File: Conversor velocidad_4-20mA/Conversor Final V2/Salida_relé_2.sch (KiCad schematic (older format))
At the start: 22 parts, among them Q2 BC848, U5 TL082

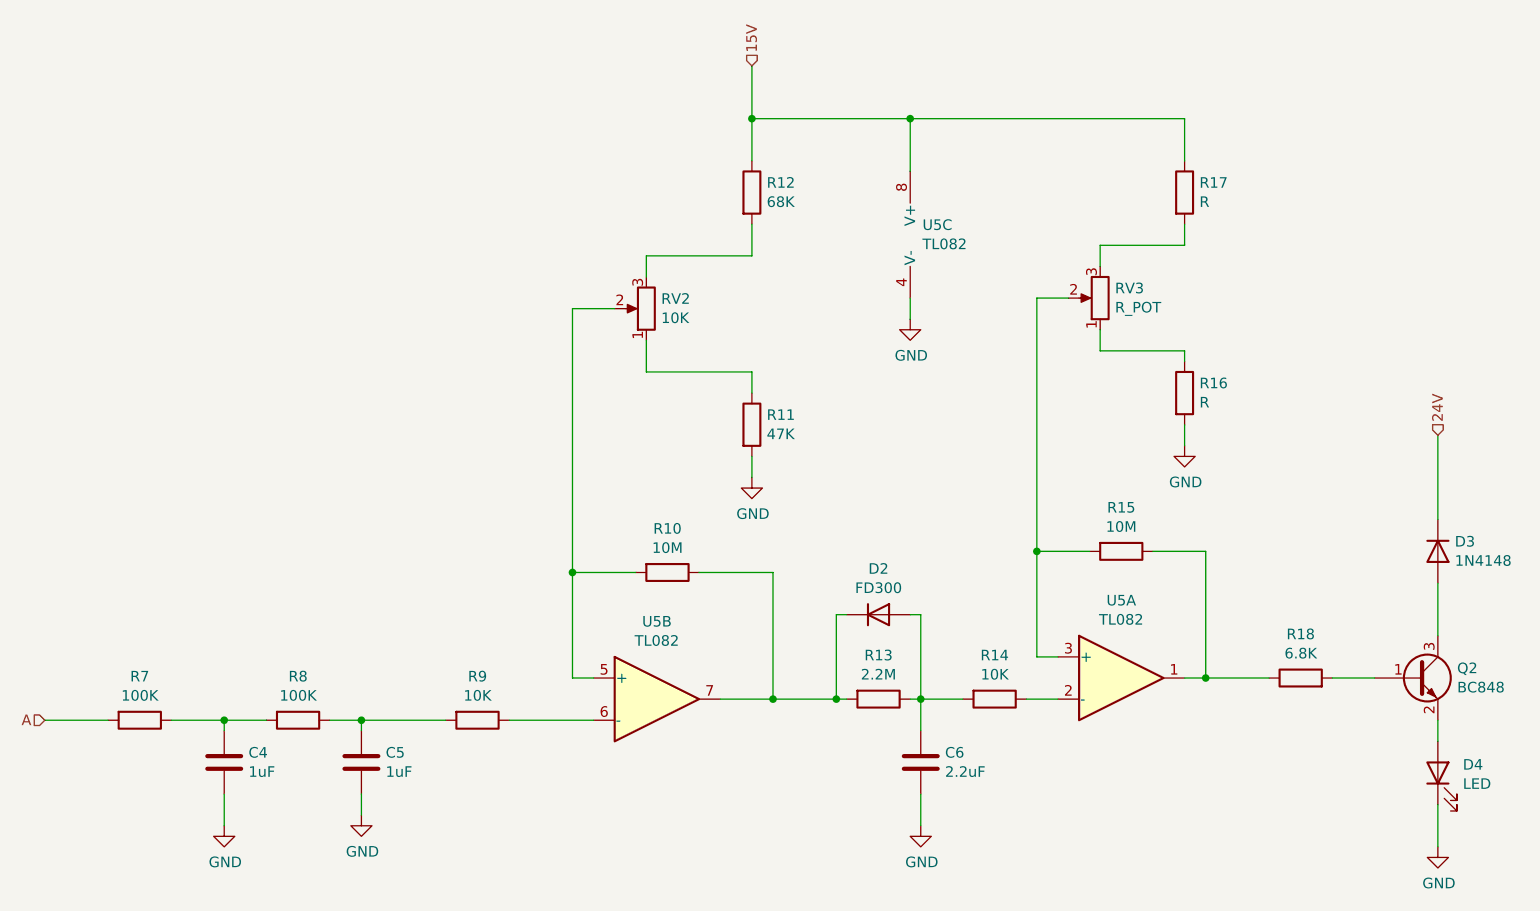
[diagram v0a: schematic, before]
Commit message: Modificacion
Modifique los esquematicos para que no de tanto error. Igualmente da error de puenteo de salidas entre las compuertas "OR" y 2 errores mas en el regulador
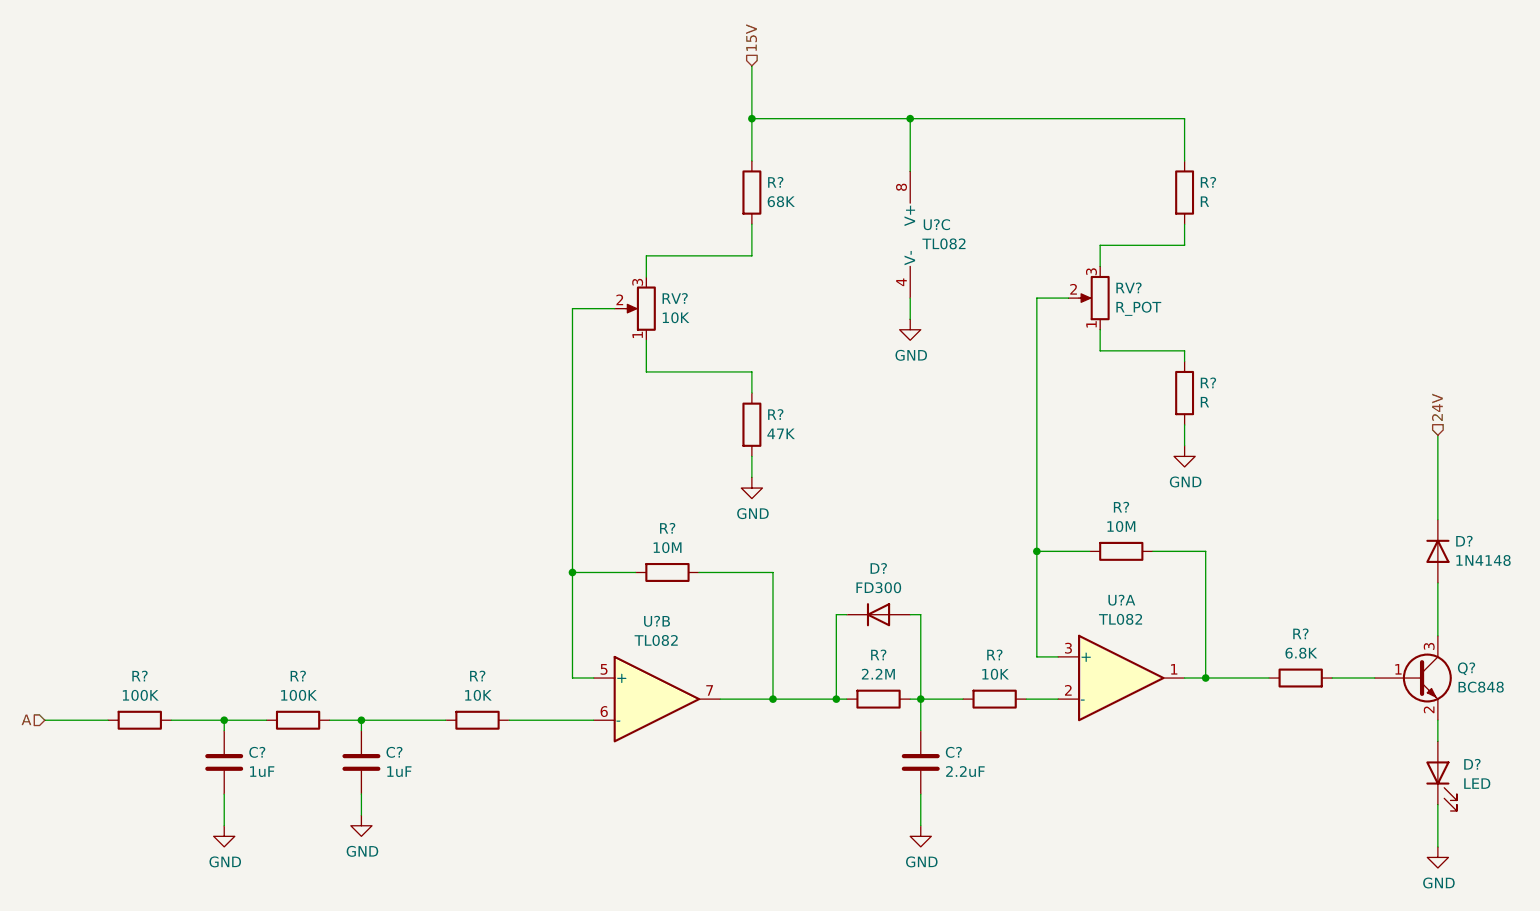
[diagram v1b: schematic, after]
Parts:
- renumbered C4 to C?, C5 to C?, C6 to C?, D2 to D?, D4 to D?, D3 to D?, Q2 to Q?, R7 to R?, R8 to R?, R9 to R?, R10 to R?, R11 to R?, R12 to R?, R13 to R?, R14 to R?, R15 to R?, R16 to R?, R17 to R?, R18 to R?, RV2 to RV?, RV3 to RV?, U5 to U?
